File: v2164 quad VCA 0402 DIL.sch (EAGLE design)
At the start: 44 parts, among them IC1 TL072JD, IC2 TL072JD, Q1 BA854SW

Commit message: Fixed some silk screen errors and replaced pads with some that solder slightly better
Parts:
- +15V, -15V, CV1, CV2, CV3, CV4, GND, IN1, IN2, IN3, IN4, OUT1, OUT2, OUT3, OUT4: device joakim:MA01-1JN -> joakim:MA01-1JP
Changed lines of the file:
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@@
 <part name="GND7" library="supply1" library_urn="urn:adsk.eagle:library:371" deviceset="GND" device=""/>
 <part name="GND8" library="supply1" library_urn="urn:adsk.eagle:library:371" deviceset="GND" device=""/>
-<part name="CV3" library="joakim" deviceset="MA01-1J" device="N"/>
-<part name="CV1" library="joakim" deviceset="MA01-1J" device="N"/>
-<part name="CV2" library="joakim" deviceset="MA01-1J" device="N"/>
-<part name="CV4" library="joakim" deviceset="MA01-1J" device="N"/>
-<part name="IN3" library="joakim" deviceset="MA01-1J" device="N"/>
-<part name="IN1" library="joakim" deviceset="MA01-1J" device="N"/>
-<part name="IN2" library="joakim" deviceset="MA01-1J" device="N"/>
-<part name="IN4" library="joakim" deviceset="MA01-1J" device="N"/>
-<part name="OUT1" library="joakim" deviceset="MA01-1J" device="N"/>
-<part name="OUT3" library="joakim" deviceset="MA01-1J" device="N"/>
-<part name="OUT4" library="joakim" deviceset="MA01-1J" device="N"/>
-<part name="OUT2" library="joakim" deviceset="MA01-1J" device="N"/>
+<part name="CV3" library="joakim" deviceset="MA01-1J" device="P"/>
+<part name="CV1" library="joakim" deviceset="MA01-1J" device="P"/>
+<part name="CV2" library="joakim" deviceset="MA01-1J" device="P"/>
+<part name="CV4" library="joakim" deviceset="MA01-1J" device="P"/>
+<part name="IN3" library="joakim" deviceset="MA01-1J" device="P"/>
+<part name="IN1" library="joakim" deviceset="MA01-1J" device="P"/>
+<part name="IN2" library="joakim" deviceset="MA01-1J" device="P"/>
+<part name="IN4" library="joakim" deviceset="MA01-1J" device="P"/>
+<part name="OUT1" library="joakim" deviceset="MA01-1J" device="P"/>
+<part name="OUT3" library="joakim" deviceset="MA01-1J" device="P"/>
+<part name="OUT4" library="joakim" deviceset="MA01-1J" device="P"/>
+<part name="OUT2" library="joakim" deviceset="MA01-1J" device="P"/>
 <part name="C11" library="rcl" library_urn="urn:adsk.eagle:library:334" deviceset="C-EU" device="C0402" package3d_urn="urn:adsk.eagle:package:23626/2" value="100nF"/>
-<part name="+15V" library="joakim" deviceset="MA01-1J" device="N"/>
-<part name="GND" library="joakim" deviceset="MA01-1J" device="N"/>
-<part name="-15V" library="joakim" deviceset="MA01-1J" device="N"/>
+<part name="+15V" library="joakim" deviceset="MA01-1J" device="P"/>
+<part name="GND" library="joakim" deviceset="MA01-1J" device="P"/>
+<part name="-15V" library="joakim" deviceset="MA01-1J" device="P"/>
 <part name="GND10" library="supply1" library_urn="urn:adsk.eagle:library:371" deviceset="GND" device=""/>
 <part name="P+2" library="supply1" library_urn="urn:adsk.eagle:library:371" deviceset="+15V" device=""/>

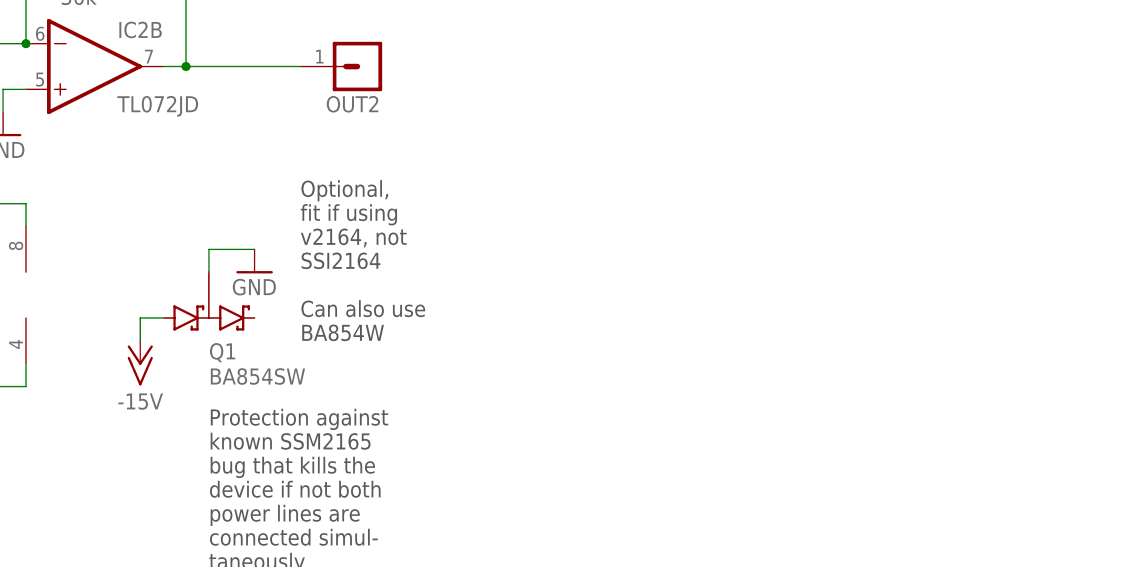
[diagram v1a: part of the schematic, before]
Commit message: Changed diode to B5817 (1n5817) as BAT854 is not available at JLCPCB
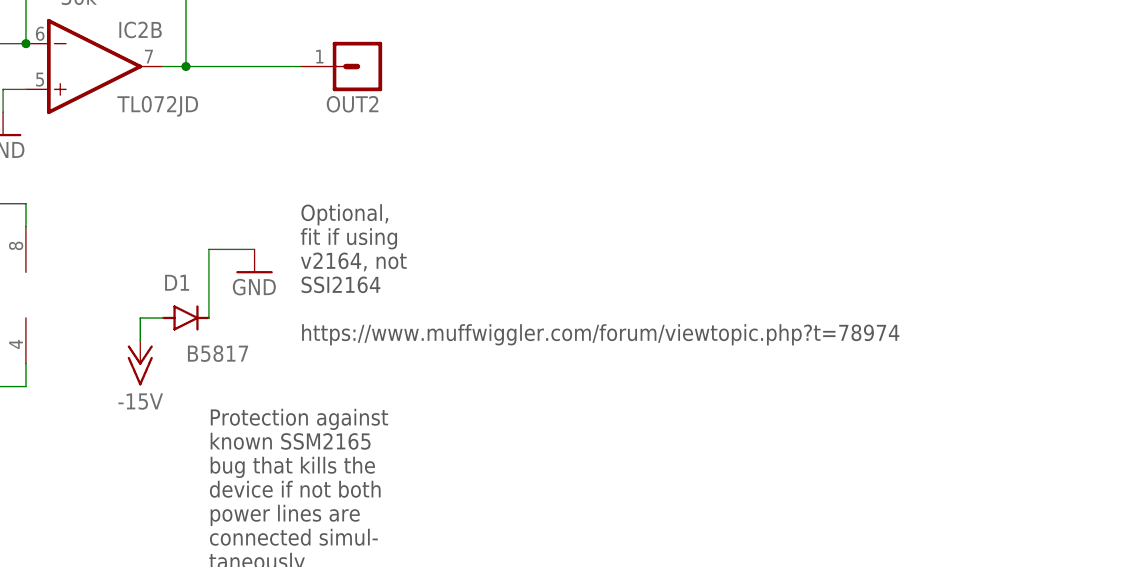
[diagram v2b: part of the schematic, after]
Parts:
- removed Q1: BA854SW, joakim:BA854SW
- added D1: B5817, diode:DIODE-SOD323-R
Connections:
- net -15V: now also D1.A; no longer Q1.A1
- net GND: now also D1.C; no longer Q1.K1A2
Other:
- note added: "Optional, fit if using v2164, not SSI2164 https://www.muffwiggler.com/forum/viewtopic.php?t=78974"
- note removed: "Optional, fit if using v2164, not SSI2164 Can also use BA854W"
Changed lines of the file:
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@@
 <part name="IC2" library="joakim" deviceset="TL072J" device="D"/>
 <part name="C12" library="rcl" library_urn="urn:adsk.eagle:library:334" deviceset="C-EU" device="C0402" package3d_urn="urn:adsk.eagle:package:23626/2" value="100nF"/>
-<part name="Q1" library="joakim" deviceset="BA854SW" device=""/>
 <part name="GND9" library="supply1" library_urn="urn:adsk.eagle:library:371" deviceset="GND" device=""/>
 <part name="P-1" library="supply1" library_urn="urn:adsk.eagle:library:371" deviceset="-15V" device=""/>
+<part name="D1" library="diode" library_urn="urn:adsk.eagle:library:210" deviceset="DIODE-" device="SOD323-R" package3d_urn="urn:adsk.eagle:package:43437/1" value="B5817"/>
 </parts>
 <sheets>
@@
 v2164, not
 SSI2164
-Can also use
-BA854W</text>
+https://www.muffwiggler.com/forum/viewtopic.php?t=78974</text>
 <text x="116.84" y="-48.26" size="1.778" layer="97">Protection against
 known SSM2165
@@
 <attribute name="VALUE" x="73.279" y="-21.336" size="1.778" layer="96" rot="R90"/>
 </instance>
-<instance part="Q1" gate="G$1" x="114.3" y="-20.32" smashed="yes">
-<attribute name="NAME" x="116.84" y="-24.9174" size="1.778" layer="95"/>
-<attribute name="VALUE" x="116.84" y="-27.7114" size="1.778" layer="96"/>
-</instance>
 <instance part="GND9" gate="1" x="121.92" y="-15.24" smashed="yes">
 <attribute name="VALUE" x="119.38" y="-17.78" size="1.778" layer="96"/>
@@
 <instance part="P-1" gate="1" x="109.22" y="-25.4" smashed="yes">
 <attribute name="VALUE" x="106.68" y="-30.48" size="1.778" layer="96"/>
+</instance>
+<instance part="D1" gate="G$1" x="114.3" y="-20.32" smashed="yes">
+<attribute name="NAME" x="111.76" y="-17.2974" size="1.778" layer="95"/>
+<attribute name="VALUE" x="114.3" y="-25.1714" size="1.778" layer="96"/>
 </instance>
 </instances>
@@
 </segment>
 <segment>
-<pinref part="Q1" gate="G$1" pin="K1A2"/>
-<wire x1="116.84" y1="-15.24" x2="116.84" y2="-12.7" width="0.1524" layer="91"/>
 <pinref part="GND9" gate="1" pin="GND"/>
 <wire x1="116.84" y1="-12.7" x2="121.92" y2="-12.7" width="0.1524" layer="91"/>
+<pinref part="D1" gate="G$1" pin="C"/>
+<wire x1="116.84" y1="-20.32" x2="116.84" y2="-12.7" width="0.1524" layer="91"/>
 </segment>
 </net>
@@
 <pinref part="P-1" gate="1" pin="-15V"/>
 <wire x1="109.22" y1="-22.86" x2="109.22" y2="-20.32" width="0.1524" layer="91"/>
-<pinref part="Q1" gate="G$1" pin="A1"/>
 <wire x1="109.22" y1="-20.32" x2="111.76" y2="-20.32" width="0.1524" layer="91"/>
-</segment>
-</net>
+<pinref part="D1" gate="G$1" pin="A"/>
+</segment>
+</net>
